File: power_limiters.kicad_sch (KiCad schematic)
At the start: 30 parts, among them U10 MAX4995AAUT+T, U11 MAX4995AAUT+T, U26 SN74AHC1G08QDCKRQ1, U35 MAX4995AAUT+T, U8 MPQ5072GG-AEC1-Z, U9 MAX4995AAUT+T

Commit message: Add licensing
Use CERN-OHL-W version 2

Signed-off-by: Corey Minyard <corey@minyard.net>
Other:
- company: (none) -> AMSAT-NA
- title: (none) -> Power Limiters
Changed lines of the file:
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@@
 	(generator_version "10.0")
 	(paper "A4")
+	(title_block
+		(title "Power Limiters")
+		(date "2026-08-20")
+		(rev "4.0")
+		(company "AMSAT-NA")
+		(comment 1 "AE5KM")
+		(comment 2 "Copyright Corey Minyard, 2026")
+		(comment 3 "Licensed under CERN-OHL-W version 2")
+	)
 	(text "= 641mA limit"
 		(exclude_from_sim no)

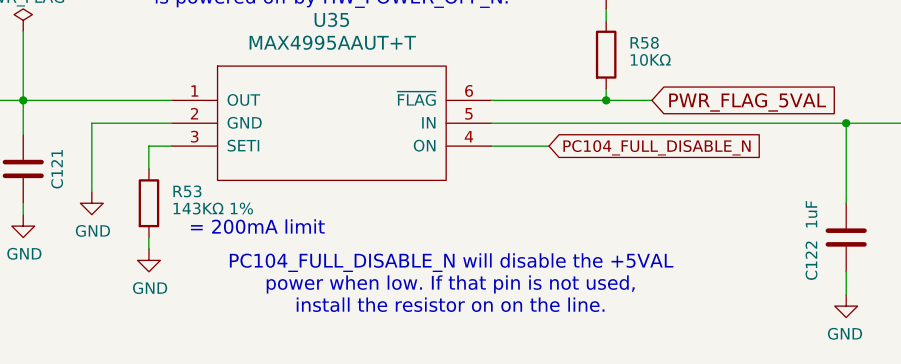
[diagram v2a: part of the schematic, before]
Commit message: Clean up some tracks, improve documentation
Add and fix a lot of documentation around the PC104 and active/standby
handling.

Signed-off-by: Corey Minyard <corey@minyard.net>
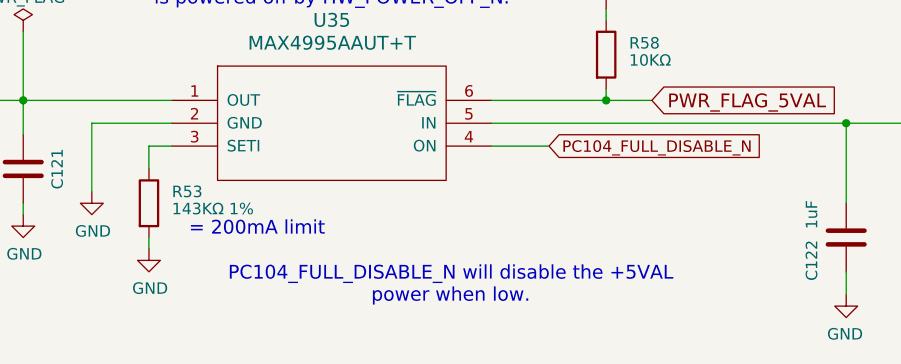
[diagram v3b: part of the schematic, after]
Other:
- note added: "PC104_FULL_DISABLE_N will disable the +5VAL power when low."
- note removed: "PC104_FULL_DISABLE_N will disable the +5VAL power when low. If that pin is not used, install the resistor on on the line."
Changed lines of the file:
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@@
 		)
 	)
-	(text "PC104_FULL_DISABLE_N will disable the +5VAL\npower when low. If that pin is not used,\ninstall the resistor on on the line."
+	(text "PC104_FULL_DISABLE_N will disable the +5VAL\npower when low."
 		(exclude_from_sim no)
 		(at 108.458 183.134 0)

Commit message: Change all leading decimal points to 0.xxx
Improve readibility.

Also add some more BOM items.

Signed-off-by: Corey Minyard <corey@minyard.net>
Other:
- note added: "0.1ms soft-start time"
- note removed: ".1ms soft-start time"
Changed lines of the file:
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@@
 		)
 	)
-	(text ".1ms soft-start time"
+	(text "0.1ms soft-start time"
 		(exclude_from_sim no)
-		(at 54.102 77.216 0)
+		(at 51.562 79.248 0)
 		(effects
 			(font

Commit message: Change all instances of K (for kilo) to k
That's the standard.

Signed-off-by: Corey Minyard <corey@minyard.net>
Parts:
- R26, R40, R41, R42, R43, R58, R64: value 10KΩ -> 10kΩ
- R36: value 47KΩ 1% -> 47kΩ 1%
- R37: value 45.3KΩ 1% -> 45.3kΩ 1%
- R38, R53: value 143KΩ 1% -> 143kΩ 1%
- R39: value 43KΩ 1% -> 43kΩ 1%
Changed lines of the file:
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@@
 			)
 		)
-		(property "Value" "143KΩ 1%"
+		(property "Value" "143kΩ 1%"
 			(at 179.07 89.535 0)
 			(show_name no)
@@
 			)
 		)
-		(property "Value" "43KΩ 1%"
+		(property "Value" "43kΩ 1%"
 			(at 179.07 128.905 0)
 			(show_name no)
@@
 			)
 		)
-		(property "Value" "45.3KΩ 1%"
+		(property "Value" "45.3kΩ 1%"
 			(at 179.07 50.165 0)
 			(show_name no)
@@
 			)
 		)
-		(property "Value" "47KΩ 1%"
+		(property "Value" "47kΩ 1%"
 			(at 24.384 94.488 90)
 			(show_name no)
@@
 			)
 		)
-		(property "Value" "10KΩ"
+		(property "Value" "10kΩ"
 			(at 218.44 89.535 0)
 			(show_name no)
@@
 			)
 		)
-		(property "Value" "10KΩ"
+		(property "Value" "10kΩ"
 			(at 218.694 129.286 0)
 			(show_name no)
@@
 			)
 		)
-		(property "Value" "10KΩ"
+		(property "Value" "10kΩ"
 			(at 217.678 70.612 0)
 			(show_name no)
@@
 			)
 		)
-		(property "Value" "10KΩ"
+		(property "Value" "10kΩ"
 			(at 83.058 120.142 0)
 			(show_name no)
@@
 			)
 		)
-		(property "Value" "10KΩ"
+		(property "Value" "10kΩ"
 			(at 128.27 158.115 0)
 			(show_name no)
@@
 			)
 		)
-		(property "Value" "10KΩ"
+		(property "Value" "10kΩ"
 			(at 229.87 112.395 0)
 			(show_name no)
@@
 			)
 		)
-		(property "Value" "143KΩ 1%"
+		(property "Value" "143kΩ 1%"
 			(at 77.47 174.625 0)
 			(show_name no)
@@
 			)
 		)
-		(property "Value" "10KΩ"
+		(property "Value" "10kΩ"
 			(at 75.438 99.822 0)
 			(show_name no)

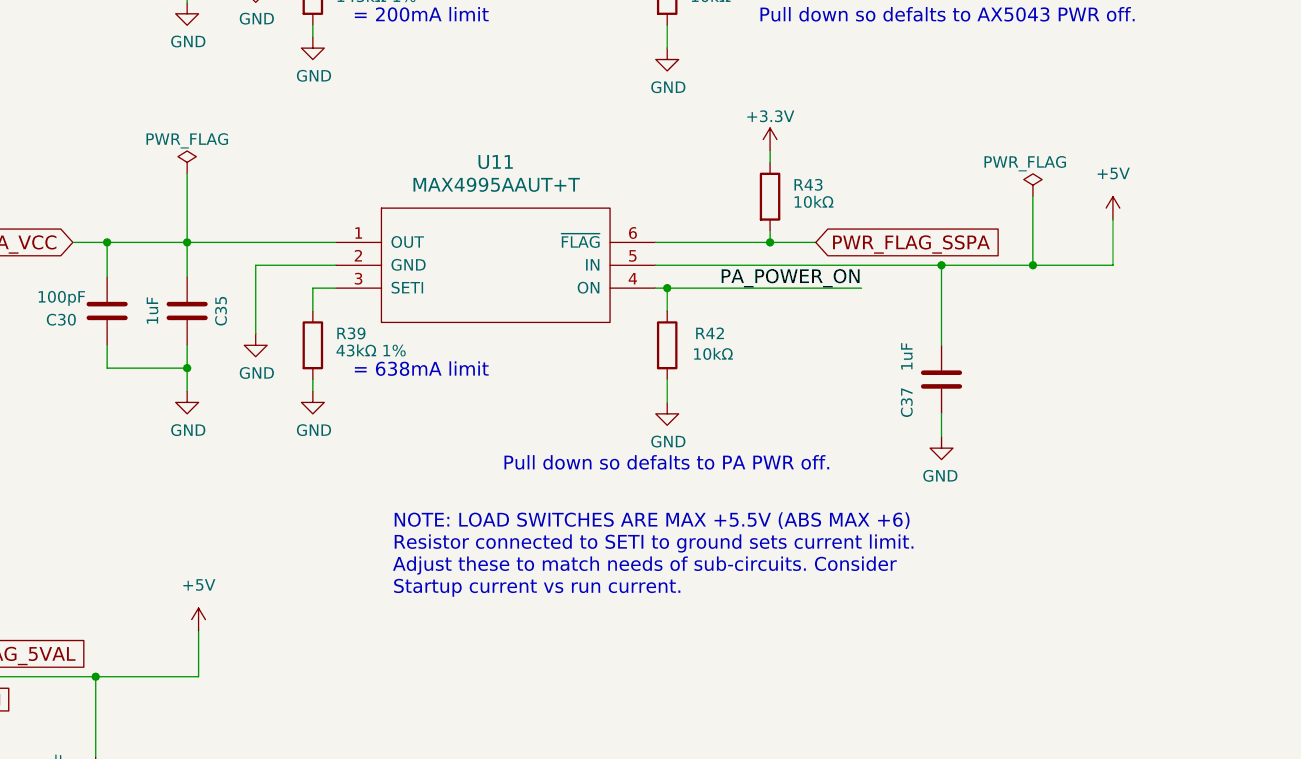
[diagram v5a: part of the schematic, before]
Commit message: Add a +5V bus for switch +5V
The +5V bus was renamed +5Vext for external power and a current
regulated +5V bus was added.  This allows latch up situations in the
CAN bus, +3.3V regulator, and a few other places to be corrected.  The
PC104_ADC4 line was converted to PWR_FLAG_5V for monitoring that
current regulator.

Signed-off-by: Corey Minyard <corey@minyard.net>
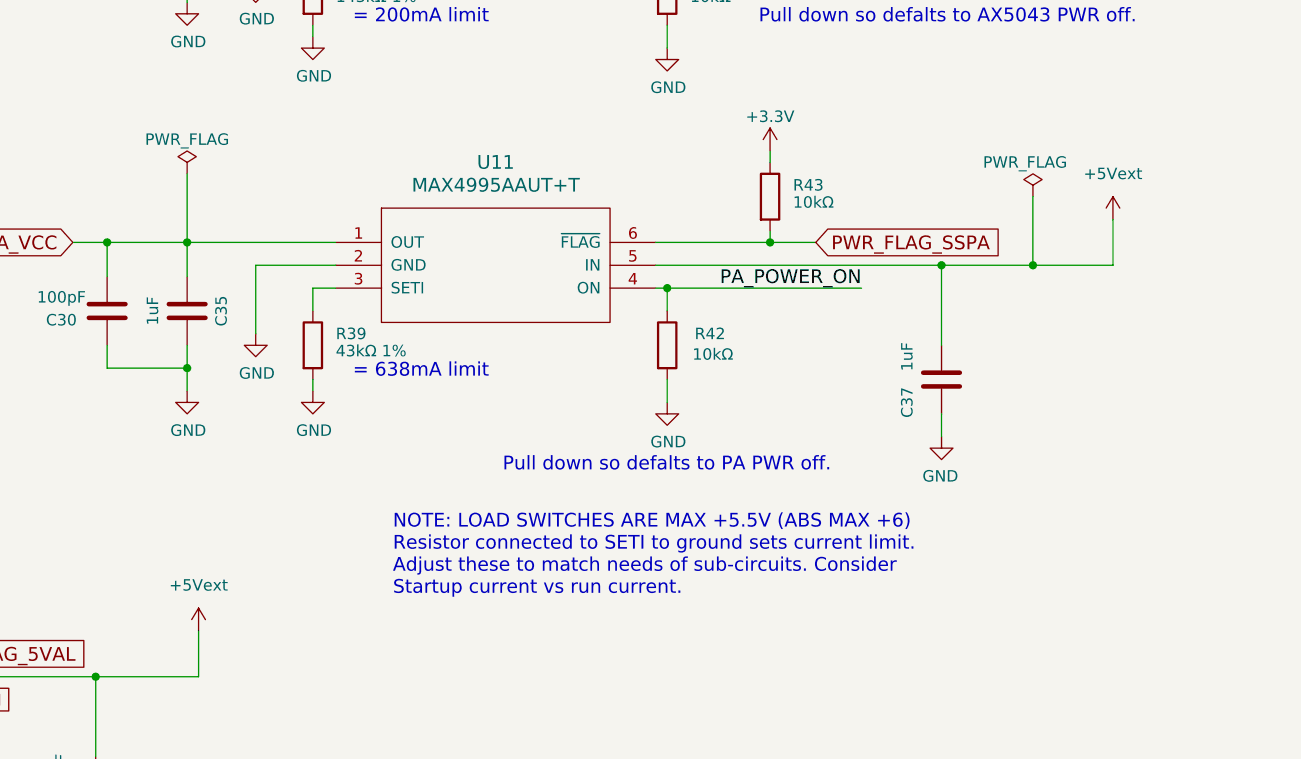
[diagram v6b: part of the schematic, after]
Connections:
- net +5V renamed +5Vext
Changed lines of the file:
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@@
 			)
 		)
-		(property "Value" "+5V"
+		(property "Value" "+5Vext"
 			(at 265.43 109.22 0)
 			(show_name no)
@@
 			)
 		)
-		(property "Value" "+5V"
+		(property "Value" "+5Vext"
 			(at 163.83 154.94 0)
 			(show_name no)

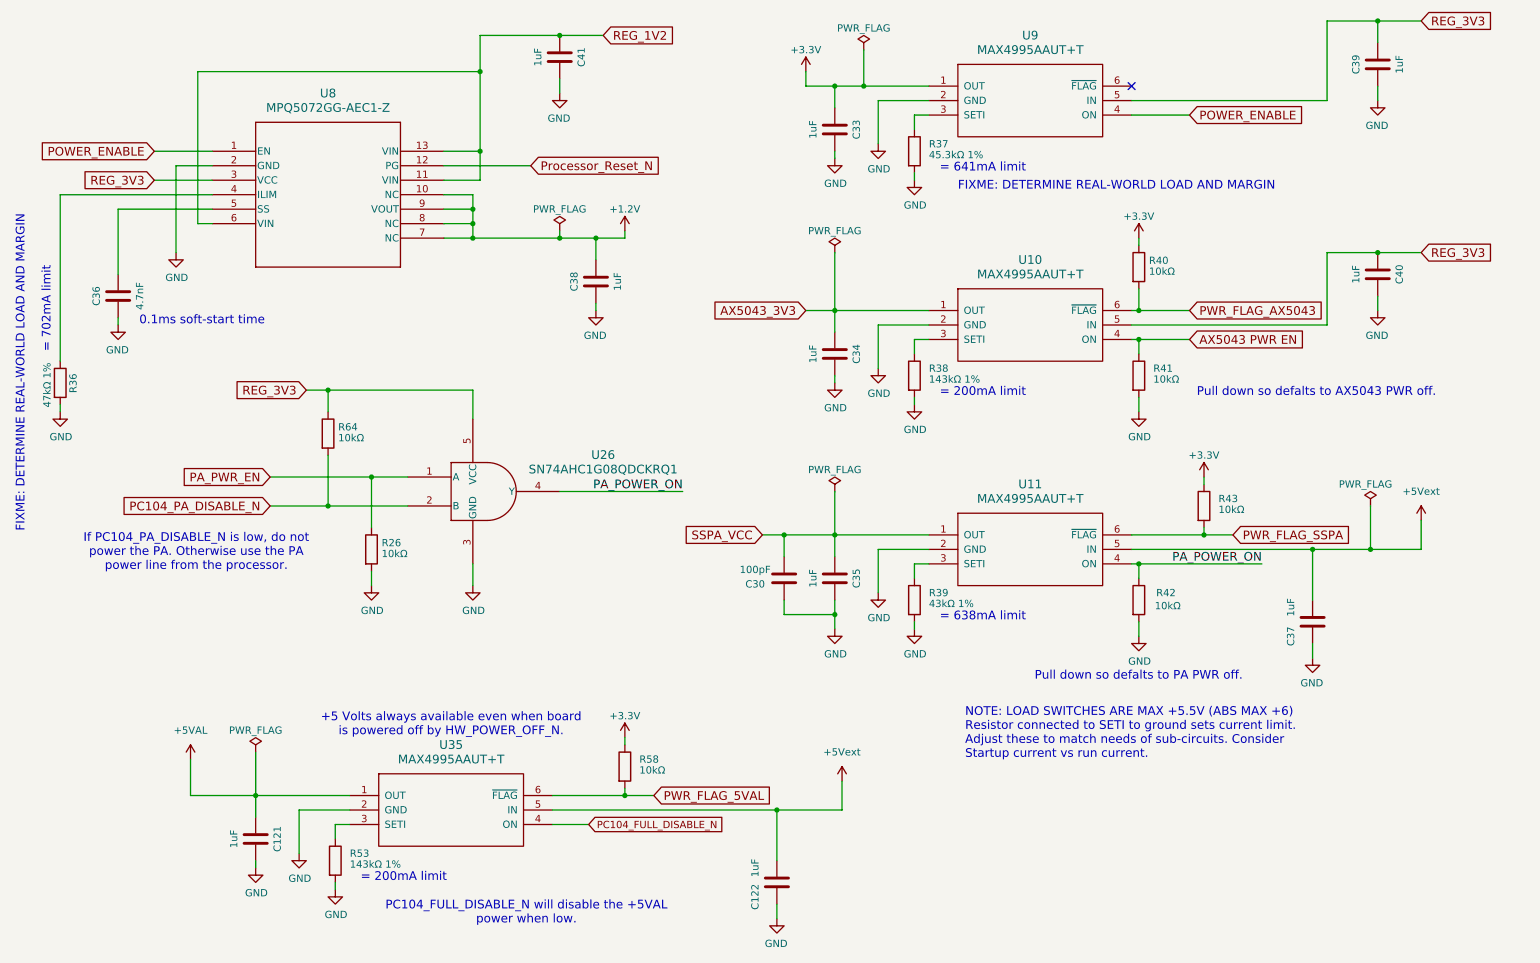
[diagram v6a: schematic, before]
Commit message: Remove PC104\_FULL\_DISABLE\_N and PC104\_PA\_DISABLE\_N
They won't be needed, and it frees up some space and some latch up
concerns.

Signed-off-by: Corey Minyard <corey@minyard.net>
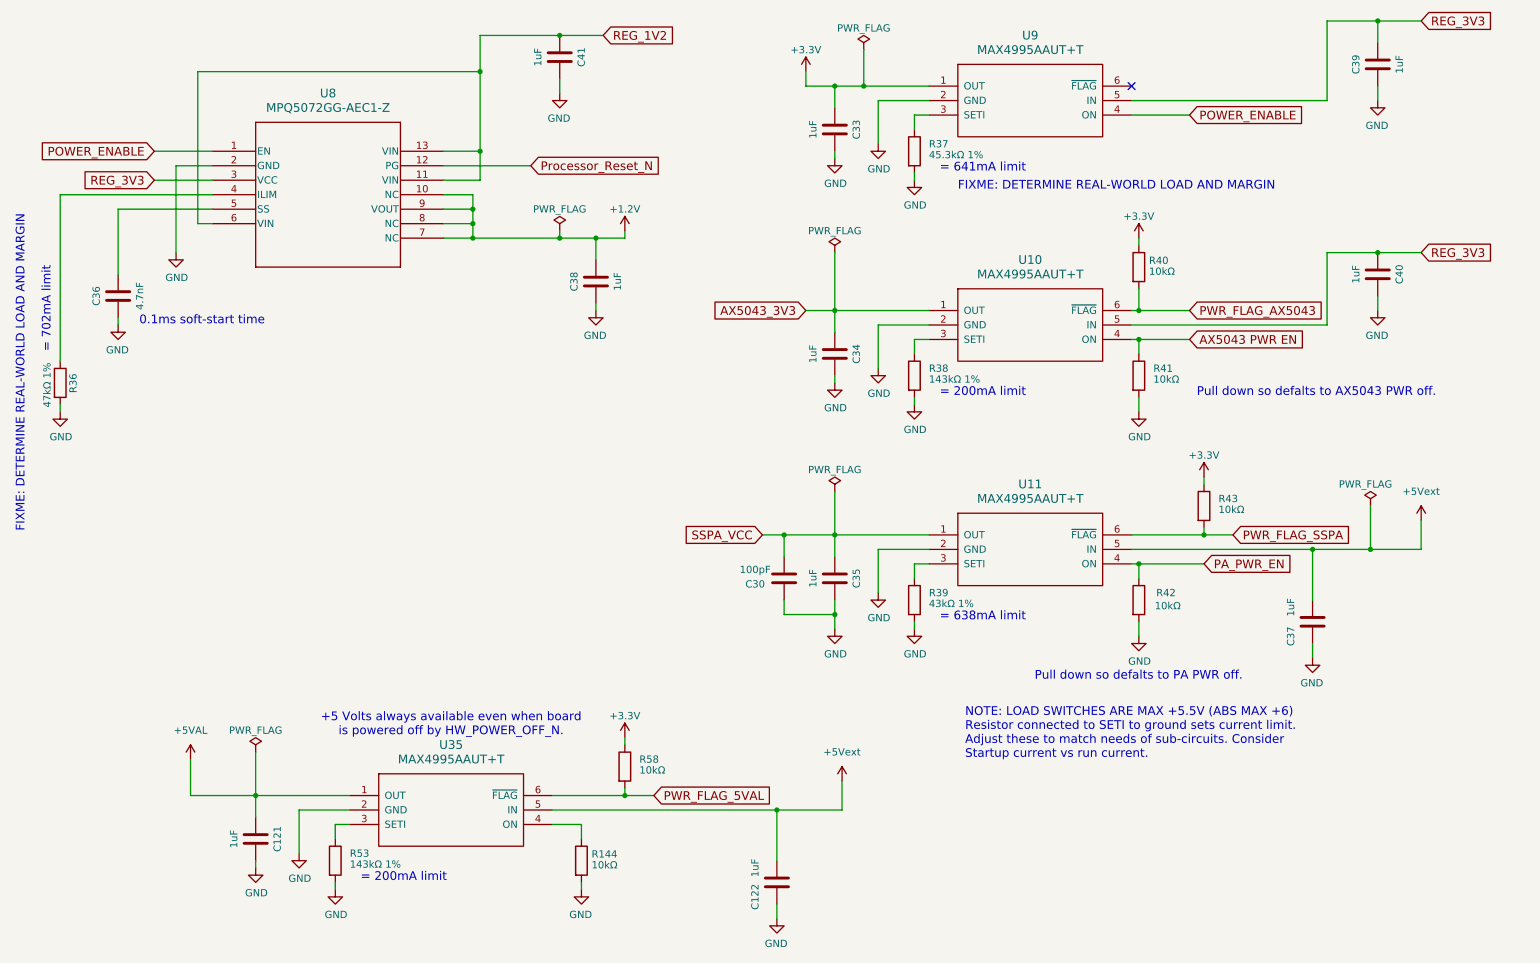
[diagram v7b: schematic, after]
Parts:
- removed R26, R64: 10kΩ, Resistor_SMD:R_0402_1005Metric_Pad0.72x0.64mm_HandSolder, symbol Device:R
- removed U26: SN74AHC1G08QDCKRQ1, PacSatDev_ti:DCK5, symbol PACSAT_ICs:SN74AHC1G08QDCKRQ1
- added R144: 10kΩ, Resistor_SMD:R_0402_1005Metric_Pad0.72x0.64mm_HandSolder, symbol Device:R
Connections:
- net PA_POWER_ON is gone; now on net PA_PWR_EN: R42.1, U11.4 (ON)
- net GND: now also R144.2
- net PC104_FULL_DISABLE_N: no longer names the net of U35.4 (ON)
- net PC104_FULL_DISABLE_N: now also R144.1
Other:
- note removed: "If PC104_PA_DISABLE_N is low, do not power the PA. Otherwise use the PA power line from the processor."
- note removed: "PC104_FULL_DISABLE_N will disable the +5VAL power when low."

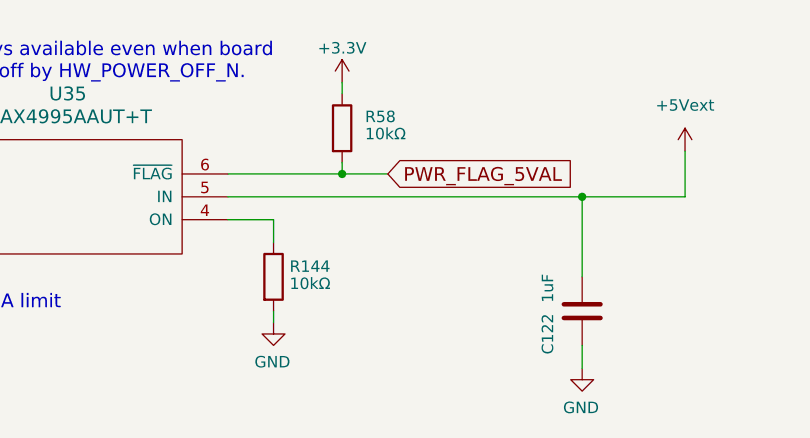
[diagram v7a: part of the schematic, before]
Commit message: Fix the enable on the +5V current limiter
It needs a pull up, not a pull down.

Signed-off-by: Corey Minyard <corey@minyard.net>
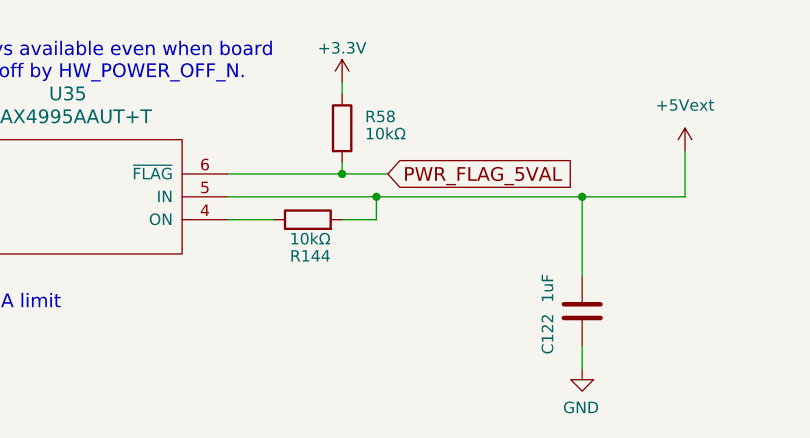
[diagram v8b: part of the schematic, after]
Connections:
- net +5Vext: now also R144.2
- net GND: no longer R144.2
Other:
- moved on the sheet: R144
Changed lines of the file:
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@@
 	)
 	(junction
+		(at 129.54 165.1)
+		(diameter 0)
+		(color 0 0 0 0)
+	)
+	(junction
 		(at 162.56 116.84)
 		(diameter 0)
@@
 	(wire
 		(pts
-			(xy 113.03 165.1) (xy 152.4 165.1)
+			(xy 113.03 165.1) (xy 129.54 165.1)
 		)
 		(stroke
@@
 	(wire
 		(pts
-			(xy 118.11 170.18) (xy 118.11 167.64)
-		)
-		(stroke
-			(width 0)
-			(type default)
-		)
-	)
-	(wire
-		(pts
 			(xy 99.06 64.77) (xy 99.06 62.23)
 		)
@@
 	(wire
 		(pts
+			(xy 129.54 167.64) (xy 129.54 165.1)
+		)
+		(stroke
+			(width 0)
+			(type default)
+		)
+	)
+	(wire
+		(pts
 			(xy 167.64 31.75) (xy 167.64 38.1)
 		)
@@
 	(wire
 		(pts
+			(xy 129.54 165.1) (xy 152.4 165.1)
+		)
+		(stroke
+			(width 0)
+			(type default)
+		)
+	)
+	(wire
+		(pts
 			(xy 99.06 57.15) (xy 99.06 59.69)
 		)
@@
 	(wire
 		(pts
+			(xy 125.73 167.64) (xy 129.54 167.64)
+		)
+		(stroke
+			(width 0)
+			(type default)
+		)
+	)
+	(wire
+		(pts
 			(xy 99.06 62.23) (xy 99.06 59.69)
 		)
@@
 	(wire
 		(pts
-			(xy 118.11 177.8) (xy 118.11 179.07)
-		)
-		(stroke
-			(width 0)
-			(type default)
-		)
-	)
-	(wire
-		(pts
 			(xy 125.73 162.56) (xy 130.81 162.56)
 		)
@@
 	)
 	(symbol
-		(lib_id "power:GND")
-		(at 118.11 179.07 0)
-		(mirror y)
-		(unit 1)
-		(body_style 1)
-		(exclude_from_sim no)
-		(in_bom yes)
-		(on_board yes)
-		(in_pos_files yes)
-		(dnp no)
-		(property "Reference" "#PWR0378"
-			(at 118.11 185.42 0)
-			(hide yes)
-			(show_name no)
-			(do_not_autoplace no)
-			(effects
-				(font
-					(size 1.27 1.27)
-				)
-			)
-		)
-		(property "Value" "GND"
-			(at 117.983 183.4642 0)
-			(show_name no)
-			(do_not_autoplace no)
-			(effects
-				(font
-					(size 1.27 1.27)
-				)
-			)
-		)
-		(property "Footprint" ""
-			(at 118.11 179.07 0)
-			(hide yes)
-			(show_name no)
-			(do_not_autoplace no)
-			(effects
-				(font
-					(size 1.27 1.27)
-				)
-			)
-		)
-		(property "Datasheet" ""
-			(at 118.11 179.07 0)
-			(hide yes)
-			(show_name no)
-			(do_not_autoplace no)
-			(effects
-				(font
-					(size 1.27 1.27)
-				)
-			)
-		)
-		(property "Description" ""
-			(at 118.11 179.07 0)
-			(show_name no)
-			(do_not_autoplace no)
-			(effects
-				(font
-					(size 1.27 1.27)
-				)
-			)
-		)
-		(pin "1"
-		)
-		(instances
-			(project "PacSat_AFSK"
-				(path "/cc9f42d2-6985-41ac-acab-5ab7b01c5b38/00000000-0000-0000-0000-00005a0ea76a/c3879c9c-e3de-4d40-a3e3-f7fd281b7d00"
-					(reference "#PWR0378")
-					(unit 1)
-				)
-			)
-		)
-	)
-	(symbol
 		(lib_id "power:+5V")
 		(at 49.53 156.21 0)
@@
 	(symbol
 		(lib_id "Device:R")
-		(at 118.11 173.99 0)
+		(at 121.92 167.64 90)
 		(unit 1)
 		(body_style 1)
@@
 		(dnp no)
 		(property "Reference" "R144"
-			(at 119.888 172.847 0)
+			(at 124.46 171.704 90)
 			(show_name no)
 			(do_not_autoplace no)
@@
 		)
 		(property "Value" "10kΩ"
-			(at 119.888 174.752 0)
+			(at 124.46 169.799 90)
 			(show_name no)
 			(do_not_autoplace no)
@@
 		)
 		(property "Footprint" "Resistor_SMD:R_0402_1005Metric_Pad0.72x0.64mm_HandSolder"
-			(at 116.332 173.99 90)
+			(at 121.92 169.418 90)
 			(hide yes)
 			(show_name no)
@@
 		)
 		(property "Datasheet" ""
-			(at 118.11 173.99 0)
+			(at 121.92 167.64 0)
 			(show_name no)
 			(do_not_autoplace no)
@@
 		)
 		(property "Description" ""
-			(at 118.11 173.99 0)
+			(at 121.92 167.64 0)
 			(show_name no)
 			(do_not_autoplace no)
